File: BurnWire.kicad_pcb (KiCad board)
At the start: 2 copper layers, 43.8 x 45.8 mm, 18 parts, among them J1 B6B-XH-A_LF__SN_, U1 ADP2303ARDZ

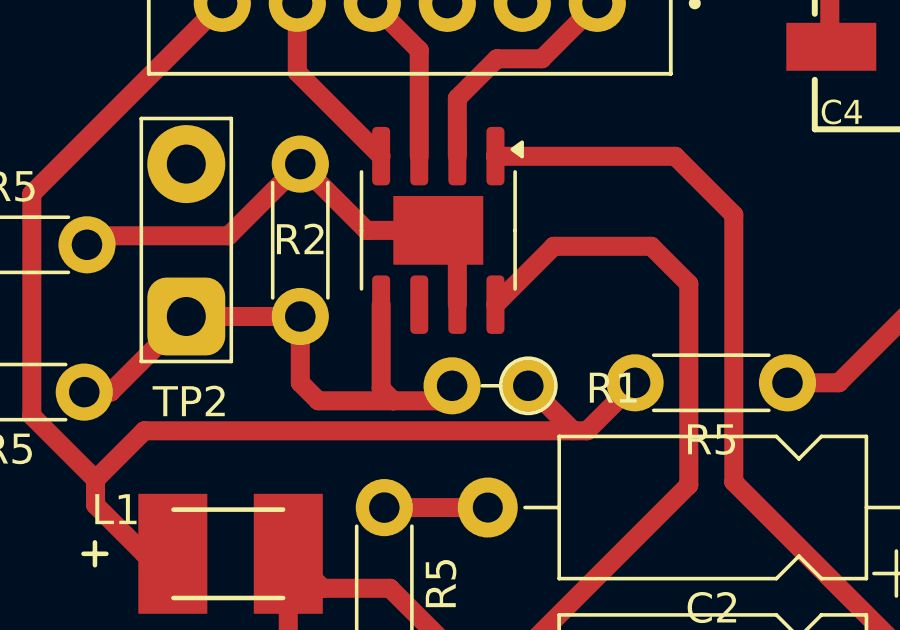
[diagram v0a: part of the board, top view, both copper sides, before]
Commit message: Polished schema w/ labels, test points; updated layout for new Vout->FB VDivider
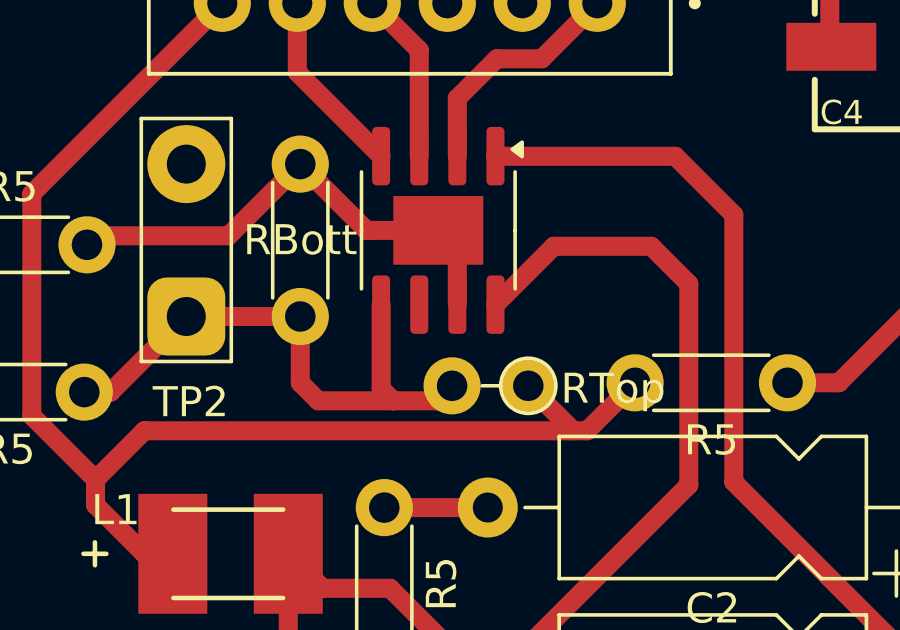
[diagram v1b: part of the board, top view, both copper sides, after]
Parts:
- renumbered R2 to RBott, R1 to RTop
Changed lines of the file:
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@@
 		(descr "Resistor, Axial_DIN0204 series, Axial, Vertical, pin pitch=2.54mm, 0.167W, length*diameter=3.6*1.6mm^2, http://cdn-reichelt.de/documents/datenblatt/B400/1_4W%23YAG.pdf")
 		(tags "Resistor Axial_DIN0204 series Axial Vertical pin pitch 2.54mm 0.167W length 3.6mm diameter 1.6mm")
-		(property "Reference" "R1"
+		(property "Reference" "RTop"
 			(at -2.83 -0.1 0)
 			(layer "F.SilkS")
@@
 		(descr "Resistor, Axial_DIN0204 series, Axial, Horizontal, pin pitch=5.08mm, 0.167W, length*diameter=3.6*1.6mm^2, http://cdn-reichelt.de/documents/datenblatt/B400/1_4W%23YAG.pdf")
 		(tags "Resistor Axial_DIN0204 series Axial Horizontal pin pitch 5.08mm 0.167W length 3.6mm diameter 1.6mm")
-		(property "Reference" "R2"
+		(property "Reference" "RBott"
 			(at 2.54 0 0)
 			(layer "F.SilkS")

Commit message: fixed R3 to correct value 100K in layout
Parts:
- R3: value 10K -> 100K
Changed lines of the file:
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@@
 			)
 		)
-		(property "Value" "10K"
+		(property "Value" "100K"
 			(at 2.54 1.92 0)
 			(layer "F.Fab")

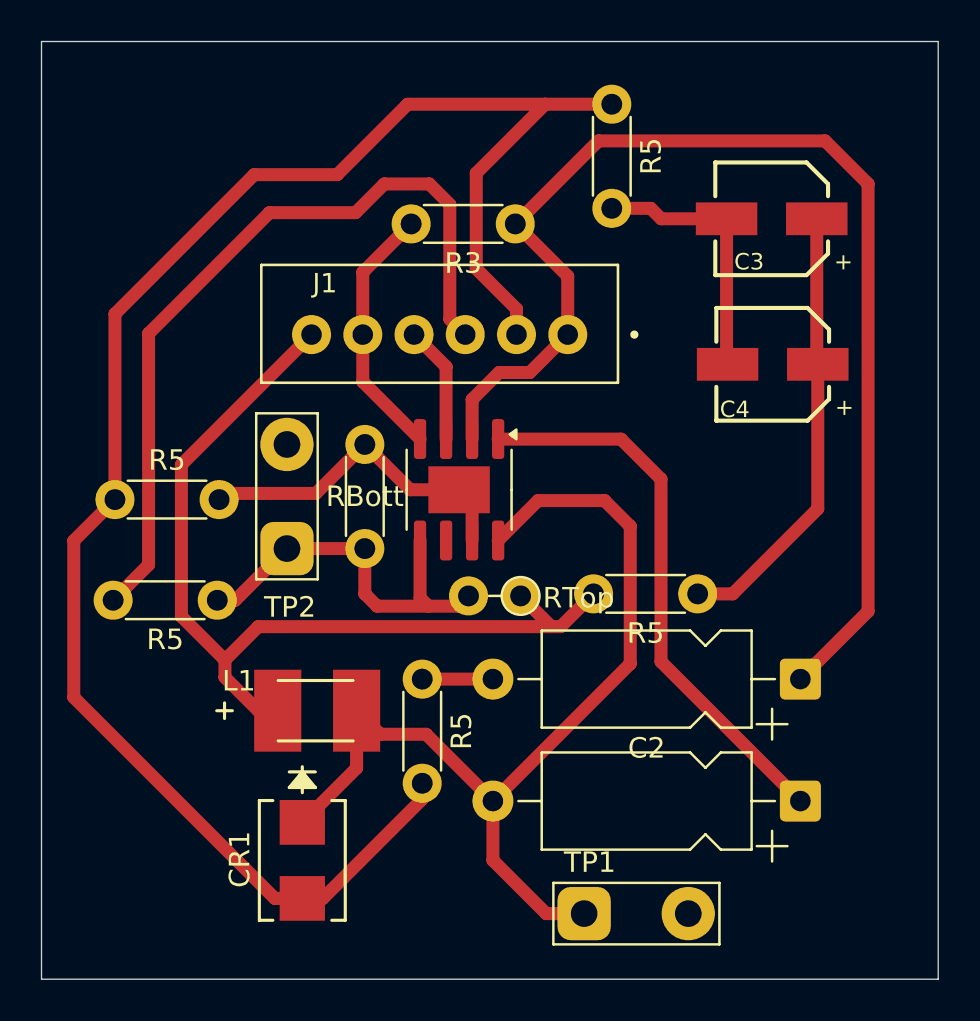
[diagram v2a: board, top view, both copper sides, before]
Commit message: Modified layout for more space
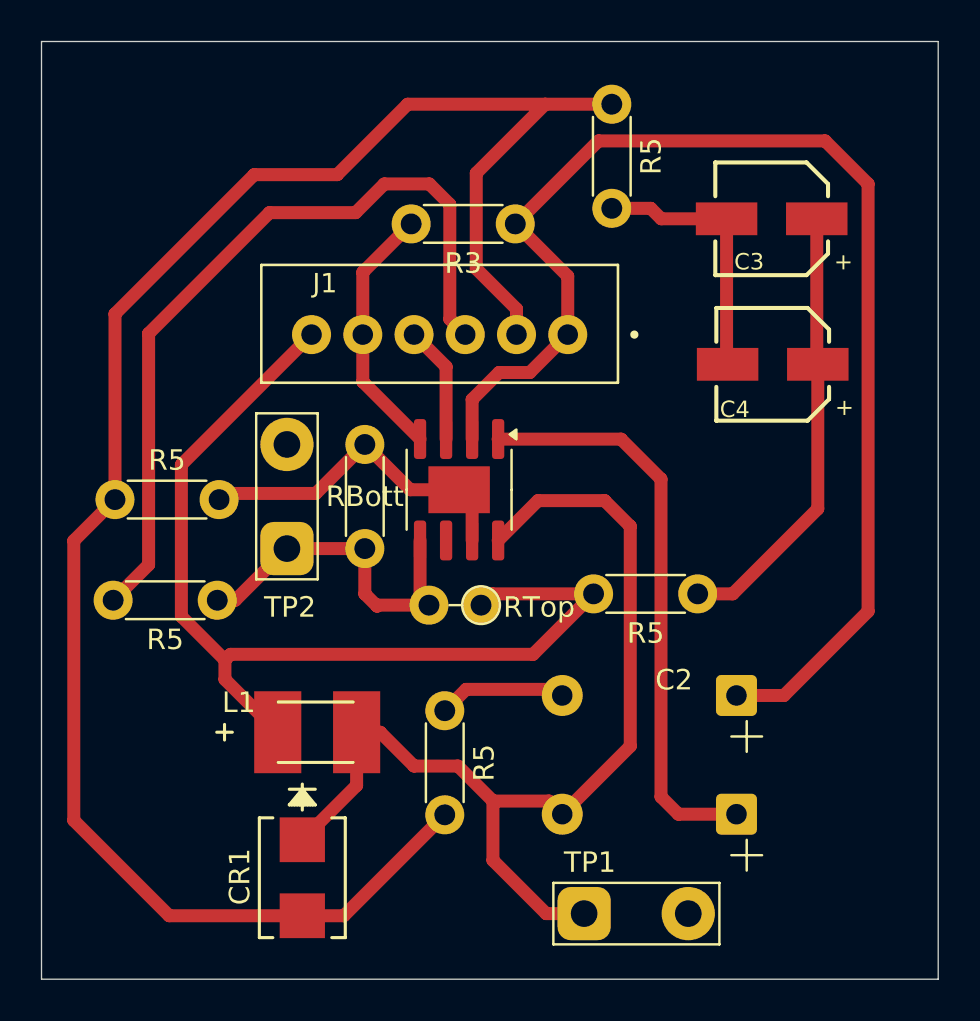
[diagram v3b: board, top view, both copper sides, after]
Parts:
- moved C1 5.41 mm to (149.3, 105.7)
- moved C2 4.19 mm to (150.5, 99.9)
- moved RTop 1.98 mm to (139.1, 95.5)
- moved R5 1.89 mm to (137.3, 100.6)
- moved L1 1.05 mm to (131.0, 101.7)
- moved CR1 0.85 mm to (130.3, 108.8)
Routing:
- net GND: track 118.2 -> 125.2 mm
- net /Vout: track 67.2 -> 70.8 mm
- net /VBatt: track 59.7 -> 63.1 mm
- net SW: track 47.4 -> 49.6 mm
- net /VCutN: track 57.9 -> 55.7 mm
- net BST: track 27.3 -> 28.3 mm

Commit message: done burnwire
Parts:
- removed L1: NLV32T-3R3J-EF, imported_footprints:IND_NLV32T_TDK
- added REF**: IND_BOURNS_SRN6045, imported_footprints:IND_BOURNS_SRN6045, F.Cu at (125.2, 101.2)
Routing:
- net SW: track 49.6 -> 58.6 mm
- net /Vout: track 70.8 -> 67.1 mm
- net /VCutN: track 55.7 -> 52.7 mm
